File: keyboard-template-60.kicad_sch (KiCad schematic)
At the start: 171 parts, among them J1 USB_C_Receptacle_USB2.0, J2 Conn_01x04_MountingPin, SW1 SW_Reset, U1 ATmega32U4-A, U2 SRV05-4, Y1 16MHz

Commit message: Assign components
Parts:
- C1, C2, C3, C4, C5, C6, C7, C8, D1, D10, D11, D12, D13, D14, D15, D16, D17, D18, D19, D2, D20, D21, D22, D24, D25, D26, D27, D28, D29, D3, D30, D31, D32, D33, D34, D35, D36, D37, D39, D4, D40, D41, D42, D43, D44, D45, D46, D47, D48, D49, D5, D50, D51, D52, D53, D54, D55, D56, D57, D58, D59, D6, D60, D61, D62, D63, D64, D65, D67, D68, D69, D7, D71, D72, D73, D74, D75, D8, D9: footprint (none) -> Diode_SMD:D_SOD-123
- F1: footprint (none) -> Fuse:Fuse_1206_3216Metric_Pad1.42x1.75mm_HandSolder
- J1: footprint (none) -> Type-C:HRO-TYPE-C-31-M-12-HandSoldering
- J2: footprint (none) -> Connector_JST:JST_SH_SM04B-SRSS-TB_1x04-1MP_P1.00mm_Horizontal
- MX1, MX10, MX11, MX12, MX13, MX14, MX15, MX16, MX17, MX18, MX19, MX2, MX20, MX21, MX22, MX24, MX25, MX26, MX27, MX28, MX29, MX3, MX30, MX32, MX33, MX34, MX35, MX36, MX37, MX38, MX38-2, MX39, MX39-2, MX4, MX40, MX41, MX42, MX43, MX44, MX45, MX46, MX47, MX48, MX49, MX5, MX50, MX51, MX52, MX53, MX54, MX55, MX56, MX57, MX58, MX59, MX6, MX60, MX61, MX62, MX63, MX63-2, MX64, MX64-2, MX65, MX65-2, MX67, MX68, MX69, MX7, MX71, MX71-2, MX72, MX72-2, MX73, MX73-2, MX74, MX75, MX8, MX9: footprint (none) -> marbastlib-mx:SW_MX_HS_1u
- R1, R2, R3, R4, R5, R6: footprint (none) -> Resistor_SMD:R_0805_2012Metric_Pad1.20x1.40mm_HandSolder
- SW1: footprint (none) -> Button_Switch_SMD:SW_SPST_SKQG_WithStem
- Y1: footprint (none) -> Crystal:Crystal_SMD_3225-4Pin_3.2x2.5mm_HandSoldering

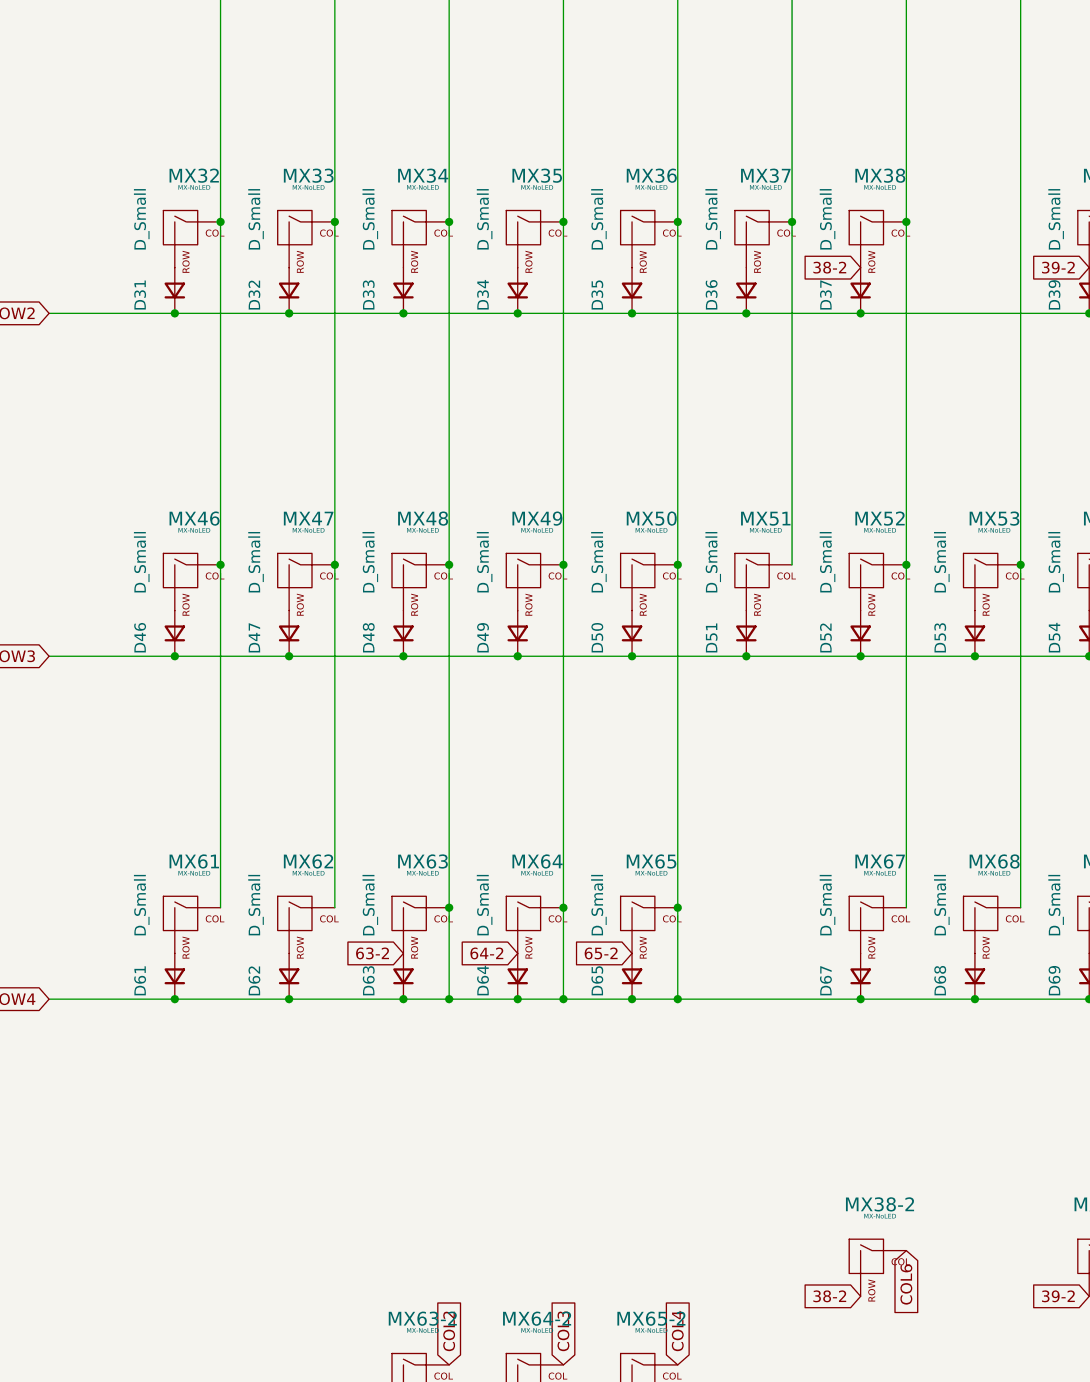
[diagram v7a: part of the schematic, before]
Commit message: Place PCB outline and parts
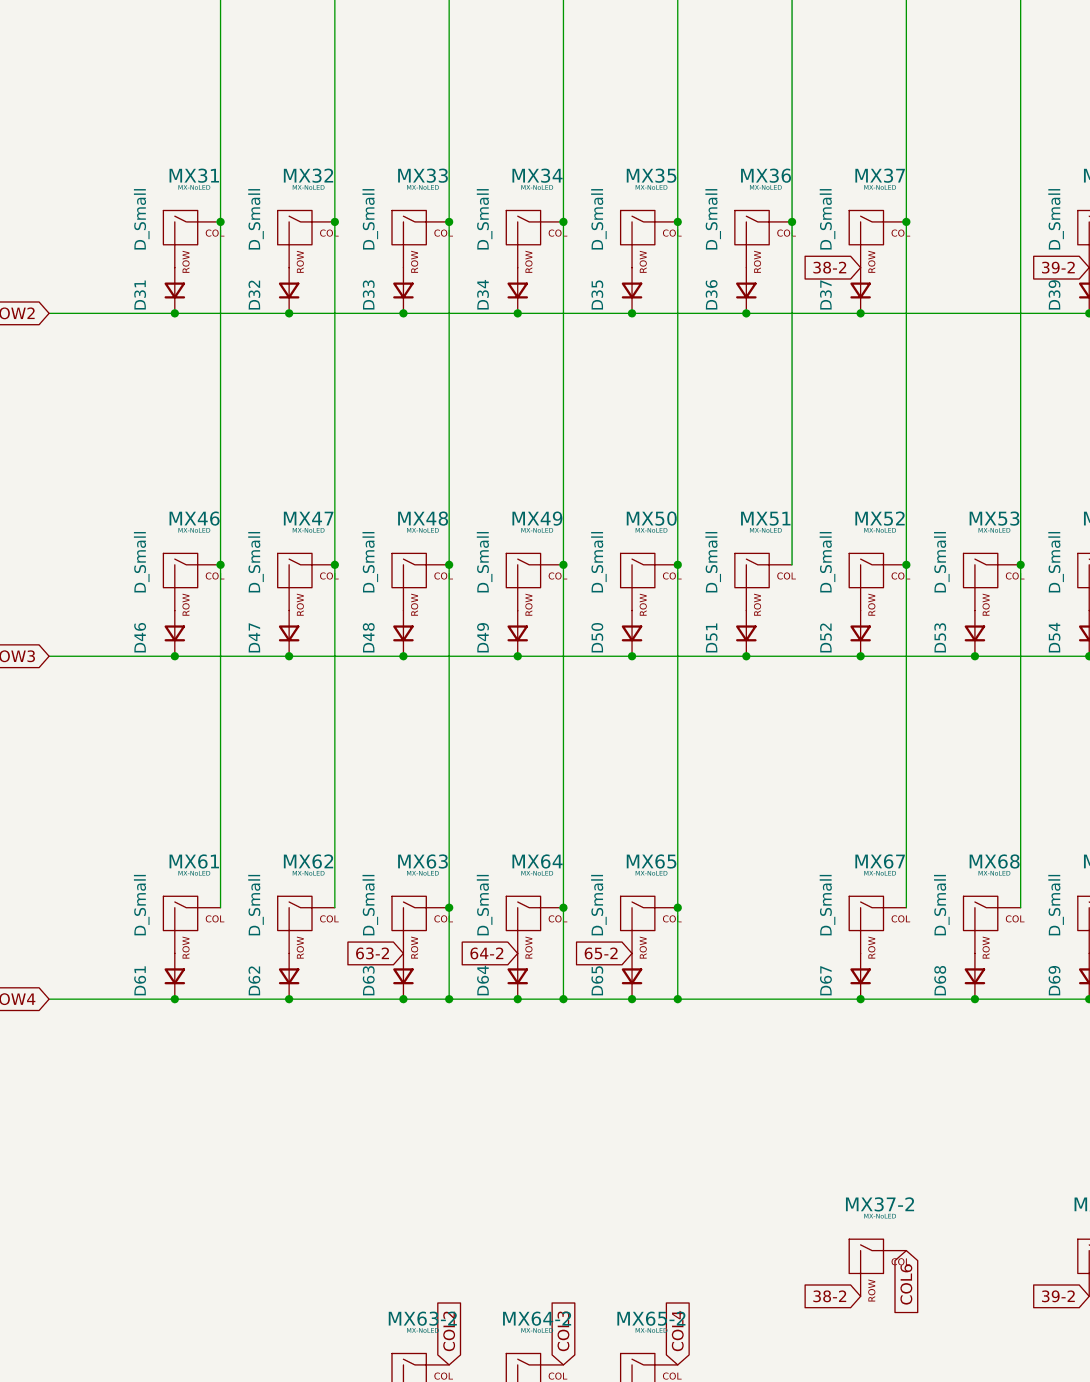
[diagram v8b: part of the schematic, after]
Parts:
- renumbered MX32 to MX31, MX33 to MX32, MX34 to MX33, MX35 to MX34, MX36 to MX35, MX37 to MX36, MX38 to MX37, MX38-2 to MX37-2
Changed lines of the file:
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@@
   (symbol (lib_id "MX_Alps_Hybrid:MX-NoLED") (at 78.74 129.54 0) (unit 1)
     (in_bom yes) (on_board yes) (fields_autoplaced)
-    (property "Reference" "MX34" (id 0) (at 79.6256 123.19 0)
+    (property "Reference" "MX33" (id 0) (at 79.6256 123.19 0)
       (effects (font (size 1.524 1.524)))
     )
@@
   (symbol (lib_id "MX_Alps_Hybrid:MX-NoLED") (at 104.14 129.54 0) (unit 1)
     (in_bom yes) (on_board yes) (fields_autoplaced)
-    (property "Reference" "MX36" (id 0) (at 105.0256 123.19 0)
+    (property "Reference" "MX35" (id 0) (at 105.0256 123.19 0)
       (effects (font (size 1.524 1.524)))
     )
@@
   (symbol (lib_id "MX_Alps_Hybrid:MX-NoLED") (at 66.04 129.54 0) (unit 1)
     (in_bom yes) (on_board yes) (fields_autoplaced)
-    (property "Reference" "MX33" (id 0) (at 66.9256 123.19 0)
+    (property "Reference" "MX32" (id 0) (at 66.9256 123.19 0)
       (effects (font (size 1.524 1.524)))
     )
@@
   (symbol (lib_id "MX_Alps_Hybrid:MX-NoLED") (at 116.84 129.54 0) (unit 1)
     (in_bom yes) (on_board yes) (fields_autoplaced)
-    (property "Reference" "MX37" (id 0) (at 117.7256 123.19 0)
+    (property "Reference" "MX36" (id 0) (at 117.7256 123.19 0)
       (effects (font (size 1.524 1.524)))
     )
@@
   (symbol (lib_id "MX_Alps_Hybrid:MX-NoLED") (at 53.34 129.54 0) (unit 1)
     (in_bom yes) (on_board yes) (fields_autoplaced)
-    (property "Reference" "MX32" (id 0) (at 54.2256 123.19 0)
+    (property "Reference" "MX31" (id 0) (at 54.2256 123.19 0)
       (effects (font (size 1.524 1.524)))
     )
@@
   (symbol (lib_id "MX_Alps_Hybrid:MX-NoLED") (at 129.54 129.54 0) (unit 1)
     (in_bom yes) (on_board yes) (fields_autoplaced)
-    (property "Reference" "MX38" (id 0) (at 130.4256 123.19 0)
+    (property "Reference" "MX37" (id 0) (at 130.4256 123.19 0)
       (effects (font (size 1.524 1.524)))
     )
@@
   (symbol (lib_id "MX_Alps_Hybrid:MX-NoLED") (at 129.54 243.84 0) (unit 1)
     (in_bom yes) (on_board yes) (fields_autoplaced)
-    (property "Reference" "MX38-2" (id 0) (at 130.4256 237.49 0)
+    (property "Reference" "MX37-2" (id 0) (at 130.4256 237.49 0)
       (effects (font (size 1.524 1.524)))
     )
@@
   (symbol (lib_id "MX_Alps_Hybrid:MX-NoLED") (at 91.44 129.54 0) (unit 1)
     (in_bom yes) (on_board yes) (fields_autoplaced)
-    (property "Reference" "MX35" (id 0) (at 92.3256 123.19 0)
+    (property "Reference" "MX34" (id 0) (at 92.3256 123.19 0)
       (effects (font (size 1.524 1.524)))
     )
@@
     )
     (path "/7b09b66a-a34b-4017-bbe5-7e28253560b5"
-      (reference "MX32") (unit 1) (value "MX-NoLED") (footprint "marbastlib-mx:SW_MX_HS_1u")
+      (reference "MX31") (unit 1) (value "MX-NoLED") (footprint "marbastlib-mx:SW_MX_HS_1u")
     )
     (path "/70703aa5-aaca-407c-bfe9-f463acb6fa92"
-      (reference "MX33") (unit 1) (value "MX-NoLED") (footprint "marbastlib-mx:SW_MX_HS_1u")
+      (reference "MX32") (unit 1) (value "MX-NoLED") (footprint "marbastlib-mx:SW_MX_HS_1u")
     )
     (path "/2124d405-00a0-4644-98e9-63c64a9c1948"
-      (reference "MX34") (unit 1) (value "MX-NoLED") (footprint "marbastlib-mx:SW_MX_HS_1u")
+      (reference "MX33") (unit 1) (value "MX-NoLED") (footprint "marbastlib-mx:SW_MX_HS_1u")
     )
     (path "/f789e8e8-c3c1-4468-9f09-3bf42b55a17b"
-      (reference "MX35") (unit 1) (value "MX-NoLED") (footprint "marbastlib-mx:SW_MX_HS_1u")
+      (reference "MX34") (unit 1) (value "MX-NoLED") (footprint "marbastlib-mx:SW_MX_HS_1u")
     )
     (path "/402e9260-223d-420a-a3d7-2ce407b472a5"
-      (reference "MX36") (unit 1) (value "MX-NoLED") (footprint "marbastlib-mx:SW_MX_HS_1u")
+      (reference "MX35") (unit 1) (value "MX-NoLED") (footprint "marbastlib-mx:SW_MX_HS_1u")
     )
     (path "/79c02b88-a8f4-4d92-b5fb-f695a6a98471"
-      (reference "MX37") (unit 1) (value "MX-NoLED") (footprint "marbastlib-mx:SW_MX_HS_1u")
+      (reference "MX36") (unit 1) (value "MX-NoLED") (footprint "marbastlib-mx:SW_MX_HS_1u")
     )
     (path "/bc635ae1-62e8-4e0b-b9cd-f1b0fba951d8"
-      (reference "MX38") (unit 1) (value "MX-NoLED") (footprint "marbastlib-mx:SW_MX_HS_1u")
+      (reference "MX37") (unit 1) (value "MX-NoLED") (footprint "marbastlib-mx:SW_MX_HS_1u")
     )
     (path "/f5c00a1c-6009-46f7-bb45-59e86d627cba"
-      (reference "MX38-2") (unit 1) (value "MX-NoLED") (footprint "marbastlib-mx:SW_MX_HS_1u")
+      (reference "MX37-2") (unit 1) (value "MX-NoLED") (footprint "marbastlib-mx:SW_MX_HS_1u")
     )
     (path "/75294b3a-bcf4-4dee-b1b0-009fd10bd357"
